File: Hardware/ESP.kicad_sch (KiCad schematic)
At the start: 22 parts, among them J2 USB_C_Receptacle_USB2.0_16P, U1 ESP32-C6-MINI-1/U, U2 TPS2115ADRBR, U8 LT1963AEST-3.3#TRPBF

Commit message: BPS-Leader Schematic completed (mostly)
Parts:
- J2: footprint UTSVT_Connectors:USB_C_Receptacle_GCT_USB4105-xx-A_16P_TopMnt_Horizontal -> UTSVT_Special:LeaderSOM
- U1: footprint (none) -> UTSVT_Special:ESP32-C6-MINI-1
- renumbered D3 to D11
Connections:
- no-connect marks 3 -> 8
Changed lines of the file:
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@@
 	)
 	(no_connect
+		(at 254 74.93)
+	)
+	(no_connect
 		(at 52.07 63.5)
 	)
@@
 	)
 	(no_connect
+		(at 254 69.85)
+	)
+	(no_connect
+		(at 254 64.77)
+	)
+	(no_connect
+		(at 254 67.31)
+	)
+	(no_connect
 		(at 52.07 60.96)
 	)
+	(no_connect
+		(at 254 72.39)
+	)
 	(wire
 		(pts
@@
 			)
 		)
-		(property "Footprint" "UTSVT_Connectors:USB_C_Receptacle_GCT_USB4105-xx-A_16P_TopMnt_Horizontal"
+		(property "Footprint" "UTSVT_Special:LeaderSOM"
 			(at 40.64 48.26 0)
 			(effects
@@
 			)
 		)
-		(property "Footprint" ""
+		(property "Footprint" "UTSVT_Special:ESP32-C6-MINI-1"
 			(at 228.6 24.13 0)
 			(effects
@@
 		(dnp no)
 		(fields_autoplaced yes)
-		(property "Reference" "D3"
+		(property "Reference" "D11"
 			(at 45.72 170.4974 90)
 			(effects
@@
 			(project "BPS-Leader"
 				(path "/fb37da34-e420-4994-8cc1-079e8c0fa48e/dabc680e-023d-4bcf-9356-bacd091b1cc9"
-					(reference "D3")
+					(reference "D11")
 					(unit 1)
 				)

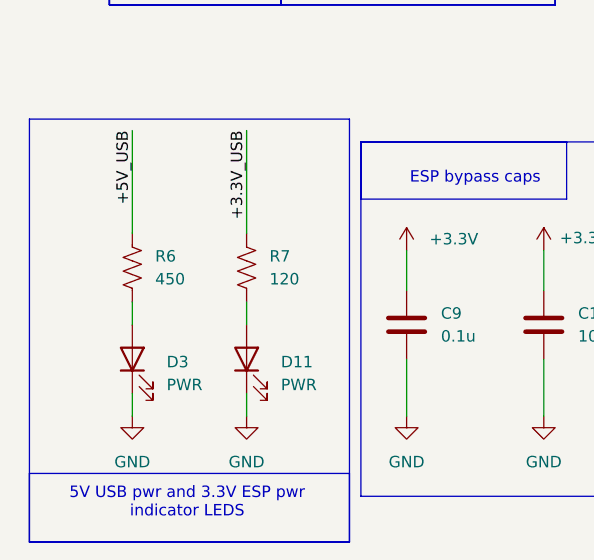
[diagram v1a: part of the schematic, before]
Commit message: added fuse, made kiCad Sharepoint a submodule, added a pulldown, added test-points
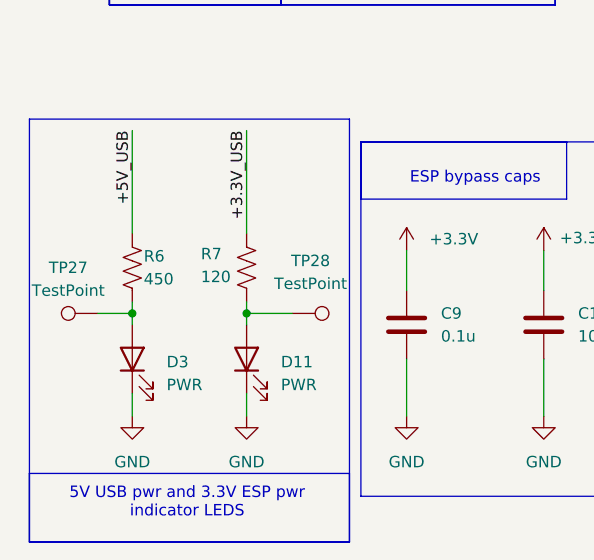
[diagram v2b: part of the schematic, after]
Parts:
- added TP27, TP28: TestPoint, symbol Connector:TestPoint
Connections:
- net at D3.2 (A), R6.2: now also TP27.1
- net at D11.2 (A), R7.2: now also TP28.1
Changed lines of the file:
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@@
 	)
 	(junction
+		(at 41.91 165.1)
+		(diameter 0)
+		(color 0 0 0 0)
+	)
+	(junction
 		(at 36.83 73.66)
 		(diameter 0)
@@
 		(color 0 0 0 0)
 	)
+	(junction
+		(at 29.21 165.1)
+		(diameter 0)
+		(color 0 0 0 0)
+	)
 	(no_connect
 		(at 254 74.93)
@@
 	(wire
 		(pts
+			(xy 41.91 165.1) (xy 41.91 166.37)
+		)
+		(stroke
+			(width 0)
+			(type default)
+		)
+	)
+	(wire
+		(pts
 			(xy 107.315 115.57) (xy 107.315 118.745)
 		)
@@
 	(wire
 		(pts
-			(xy 41.91 163.83) (xy 41.91 166.37)
+			(xy 41.91 163.83) (xy 41.91 165.1)
+		)
+		(stroke
+			(width 0)
+			(type default)
+		)
+	)
+	(wire
+		(pts
+			(xy 41.91 165.1) (xy 46.99 165.1)
 		)
 		(stroke
@@
 	(wire
 		(pts
-			(xy 29.21 163.83) (xy 29.21 166.37)
+			(xy 29.21 163.83) (xy 29.21 165.1)
 		)
 		(stroke
@@
 	(wire
 		(pts
+			(xy 25.4 165.1) (xy 29.21 165.1)
+		)
+		(stroke
+			(width 0)
+			(type default)
+		)
+	)
+	(wire
+		(pts
 			(xy 54.61 53.34) (xy 63.5 53.34)
 		)
@@
 	(wire
 		(pts
+			(xy 29.21 165.1) (xy 29.21 166.37)
+		)
+		(stroke
+			(width 0)
+			(type default)
+		)
+	)
+	(wire
+		(pts
 			(xy 41.91 144.78) (xy 41.91 156.21)
 		)
@@
 		(on_board yes)
 		(dnp no)
-		(fields_autoplaced yes)
 		(property "Reference" "R6"
-			(at 31.75 158.7499 0)
+			(at 30.48 158.75 0)
 			(effects
 				(font
@@
 		)
 		(property "Value" "450"
-			(at 31.75 161.2899 0)
+			(at 30.48 161.29 0)
 			(effects
 				(font
@@
 		(on_board yes)
 		(dnp no)
-		(fields_autoplaced yes)
 		(property "Reference" "R7"
-			(at 44.45 158.7499 0)
+			(at 36.83 158.496 0)
 			(effects
 				(font
@@
 		)
 		(property "Value" "120"
-			(at 44.45 161.2899 0)
+			(at 36.83 161.036 0)
 			(effects
 				(font
@@
 	)
 	(symbol
+		(lib_id "Connector:TestPoint")
+		(at 25.4 165.1 90)
+		(unit 1)
+		(exclude_from_sim no)
+		(in_bom yes)
+		(on_board yes)
+		(dnp no)
+		(fields_autoplaced yes)
+		(property "Reference" "TP27"
+			(at 22.098 160.02 90)
+			(effects
+				(font
+					(size 1.27 1.27)
+				)
+			)
+		)
+		(property "Value" "TestPoint"
+			(at 22.098 162.56 90)
+			(effects
+				(font
+					(size 1.27 1.27)
+				)
+			)
+		)
+		(property "Footprint" ""
+			(at 25.4 160.02 0)
+			(effects
+				(font
+					(size 1.27 1.27)
+				)
+				(hide yes)
+			)
+		)
+		(property "Datasheet" "~"
+			(at 25.4 160.02 0)
+			(effects
+				(font
+					(size 1.27 1.27)
+				)
+				(hide yes)
+			)
+		)
+		(property "Description" "test point"
+			(at 25.4 165.1 0)
+			(effects
+				(font
+					(size 1.27 1.27)
+				)
+				(hide yes)
+			)
+		)
+		(pin "1"
+		)
+		(instances
+			(project ""
+				(path "/fb37da34-e420-4994-8cc1-079e8c0fa48e/dabc680e-023d-4bcf-9356-bacd091b1cc9"
+					(reference "TP27")
+					(unit 1)
+				)
+			)
+		)
+	)
+	(symbol
 		(lib_id "Device:C")
 		(at 116.84 124.46 0)
@@
 					(unit 1)
 				)
+			)
+		)
+	)
+	(symbol
+		(lib_id "Connector:TestPoint")
+		(at 46.99 165.1 270)
+		(mirror x)
+		(unit 1)
+		(exclude_from_sim no)
+		(in_bom yes)
+		(on_board yes)
+		(dnp no)
+		(property "Reference" "TP28"
+			(at 49.022 159.258 90)
+			(effects
+				(font
+					(size 1.27 1.27)
+				)
+			)
+		)
+		(property "Value" "TestPoint"
+			(at 49.022 161.798 90)
+			(effects
+				(font
+					(size 1.27 1.27)
+				)
+			)
+		)
+		(property "Footprint" ""
+			(at 46.99 160.02 0)
+			(effects
+				(font
+					(size 1.27 1.27)
+				)
+				(hide yes)
+			)
+		)
+		(property "Datasheet" "~"
+			(at 46.99 160.02 0)
+			(effects
+				(font
+					(size 1.27 1.27)
+				)
+				(hide yes)
+			)
+		)
+		(property "Description" "test point"
+			(at 46.99 165.1 0)
+			(effects
+				(font
+					(size 1.27 1.27)
+				)
+				(hide yes)
+			)
+		)
+		(pin "1"
+		)
+		(instances
+			(project "BPS-Leader"
+				(path "/fb37da34-e420-4994-8cc1-079e8c0fa48e/dabc680e-023d-4bcf-9356-bacd091b1cc9"
+					(reference "TP28")
+					(unit 1)
+				)

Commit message: Small tweaks
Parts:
- added TP47, TP48: TestPoint, UTSVT_Special:TestPoint_HEX_3mmID, symbol Connector:TestPoint
- TP27, TP28: footprint (none) -> UTSVT_Special:TestPoint_HEX_3mmID
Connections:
- net +3.3V_USB: now also TP47.1
- net +5V_USB: now also TP48.1
- net +3.3V renamed +3.3V_ESP
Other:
- note added: "This is taken from VCU's ESP.kicad_sch (circa 09/09/2025) Only minimal cosmetic changes were made (i.e. 3V3 to +3.3V)"
- note removed: "This is taken from VCU's ESP.kicad_sch (circa 09/09/2025) Only minimal cosmetic changes were made (i.e. 3V3 to +3.3V) NOTE TO AUTHOR: CONFIRM PART DESIGNATION PARITY (i.e. J1 and U2)"
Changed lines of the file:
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@@
 	)
 	(rectangle
-		(start 17.78 143.51)
+		(start 16.002 143.51)
 		(end 53.34 190.5)
 		(stroke
@@
 		)
 	)
-	(text "This is taken from VCU's ESP.kicad_sch (circa 09/09/2025) \nOnly minimal cosmetic changes were made (i.e. 3V3 to +3.3V)\nNOTE TO AUTHOR: CONFIRM PART DESIGNATION PARITY (i.e. J1 and U2)"
+	(text "This is taken from VCU's ESP.kicad_sch (circa 09/09/2025) \nOnly minimal cosmetic changes were made (i.e. 3V3 to +3.3V)\n"
 		(exclude_from_sim no)
 		(at 214.884 172.212 0)
@@
 	)
 	(junction
+		(at 29.21 154.94)
+		(diameter 0)
+		(color 0 0 0 0)
+	)
+	(junction
 		(at 123.825 146.05)
 		(diameter 0)
@@
 	)
 	(junction
+		(at 41.91 153.67)
+		(diameter 0)
+		(color 0 0 0 0)
+	)
+	(junction
 		(at 116.84 118.11)
 		(diameter 0)
@@
 	(wire
 		(pts
+			(xy 41.91 153.67) (xy 41.91 156.21)
+		)
+		(stroke
+			(width 0)
+			(type default)
+		)
+	)
+	(wire
+		(pts
 			(xy 254 54.61) (xy 264.16 54.61)
 		)
@@
 	(wire
 		(pts
-			(xy 41.91 144.78) (xy 41.91 156.21)
+			(xy 41.91 144.78) (xy 41.91 153.67)
 		)
 		(stroke
@@
 	(wire
 		(pts
+			(xy 26.67 154.94) (xy 29.21 154.94)
+		)
+		(stroke
+			(width 0)
+			(type default)
+		)
+	)
+	(wire
+		(pts
 			(xy 226.06 85.09) (xy 226.06 90.17)
 		)
@@
 	(wire
 		(pts
-			(xy 29.21 144.78) (xy 29.21 156.21)
+			(xy 29.21 144.78) (xy 29.21 154.94)
 		)
 		(stroke
@@
 	(wire
 		(pts
+			(xy 29.21 154.94) (xy 29.21 156.21)
+		)
+		(stroke
+			(width 0)
+			(type default)
+		)
+	)
+	(wire
+		(pts
 			(xy 250.19 118.745) (xy 260.35 118.745)
 		)
@@
 		)
 	)
+	(wire
+		(pts
+			(xy 44.45 153.67) (xy 41.91 153.67)
+		)
+		(stroke
+			(width 0)
+			(type default)
+		)
+	)
 	(label "IO12"
 		(at 187.96 41.91 0)
@@
 			)
 		)
-		(property "Value" "+3.3V"
+		(property "Value" "+3.3V_ESP"
 			(at 226.06 17.78 0)
 			(effects
@@
 	)
 	(symbol
+		(lib_id "Connector:TestPoint")
+		(at 26.67 154.94 90)
+		(unit 1)
+		(exclude_from_sim no)
+		(in_bom yes)
+		(on_board yes)
+		(dnp no)
+		(property "Reference" "TP48"
+			(at 20.574 150.622 90)
+			(effects
+				(font
+					(size 1.27 1.27)
+				)
+			)
+		)
+		(property "Value" "TestPoint"
+			(at 21.082 152.908 90)
+			(effects
+				(font
+					(size 1.27 1.27)
+				)
+			)
+		)
+		(property "Footprint" "UTSVT_Special:TestPoint_HEX_3mmID"
+			(at 26.67 149.86 0)
+			(effects
+				(font
+					(size 1.27 1.27)
+				)
+				(hide yes)
+			)
+		)
+		(property "Datasheet" "~"
+			(at 26.67 149.86 0)
+			(effects
+				(font
+					(size 1.27 1.27)
+				)
+				(hide yes)
+			)
+		)
+		(property "Description" "test point"
+			(at 26.67 154.94 0)
+			(effects
+				(font
+					(size 1.27 1.27)
+				)
+				(hide yes)
+			)
+		)
+		(pin "1"
+		)
+		(instances
+			(project "BPS-Leader"
+				(path "/fb37da34-e420-4994-8cc1-079e8c0fa48e/dabc680e-023d-4bcf-9356-bacd091b1cc9"
+					(reference "TP48")
+					(unit 1)
+				)
+			)
+		)
+	)
+	(symbol
 		(lib_id "Device:R_US")
 		(at 29.21 160.02 0)
@@
 			)
 		)
-		(property "Value" "+3.3V"
-			(at 182.245 114.2999 0)
+		(property "Value" "+3.3V_ESP"
+			(at 176.784 111.76 0)
 			(effects
 				(font
@@
 			)
 		)
-		(property "Footprint" ""
+		(property "Footprint" "UTSVT_Special:TestPoint_HEX_3mmID"
 			(at 25.4 160.02 0)
 			(effects
@@
 		(dnp no)
 		(fields_autoplaced yes)
-		(property "Reference" "#PWR070"
+		(property "Reference" "#+3.3V_ESP0101"
 			(at 59.69 161.925 0)
 			(effects
@@
 			)
 		)
-		(property "Value" "+3.3V"
+		(property "Value" "+3.3V_ESP"
 			(at 62.23 156.8449 0)
 			(effects
@@
 			(project "BPS-Leader"
 				(path "/fb37da34-e420-4994-8cc1-079e8c0fa48e/dabc680e-023d-4bcf-9356-bacd091b1cc9"
-					(reference "#PWR070")
+					(reference "#+3.3V_ESP0101")
 					(unit 1)
 				)
@@
 	)
 	(symbol
+		(lib_id "Connector:TestPoint")
+		(at 44.45 153.67 270)
+		(mirror x)
+		(unit 1)
+		(exclude_from_sim no)
+		(in_bom yes)
+		(on_board yes)
+		(dnp no)
+		(property "Reference" "TP47"
+			(at 46.482 147.828 90)
+			(effects
+				(font
+					(size 1.27 1.27)
+				)
+			)
+		)
+		(property "Value" "TestPoint"
+			(at 46.482 150.368 90)
+			(effects
+				(font
+					(size 1.27 1.27)
+				)
+			)
+		)
+		(property "Footprint" "UTSVT_Special:TestPoint_HEX_3mmID"
+			(at 44.45 148.59 0)
+			(effects
+				(font
+					(size 1.27 1.27)
+				)
+				(hide yes)
+			)
+		)
+		(property "Datasheet" "~"
+			(at 44.45 148.59 0)
+			(effects
+				(font
+					(size 1.27 1.27)
+				)
+				(hide yes)
+			)
+		)
+		(property "Description" "test point"
+			(at 44.45 153.67 0)
+			(effects
+				(font
+					(size 1.27 1.27)
+				)
+				(hide yes)
+			)
+		)
+		(pin "1"
+		)
+		(instances
+			(project "BPS-Leader"
+				(path "/fb37da34-e420-4994-8cc1-079e8c0fa48e/dabc680e-023d-4bcf-9356-bacd091b1cc9"
+					(reference "TP47")
+					(unit 1)
+				)
+			)
+		)
+	)
+	(symbol
 		(lib_id "power:GND")
 		(at 74.93 176.53 0)
@@
 			)
 		)
-		(property "Footprint" ""
+		(property "Footprint" "UTSVT_Special:TestPoint_HEX_3mmID"
 			(at 46.99 160.02 0)
 			(effects
@@
 			)
 		)
-		(property "Value" "+3.3V"
+		(property "Value" "+3.3V_ESP"
 			(at 76.708 156.718 0)
 			(effects

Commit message: Very, very intial layout designed. Many issues. Too bad!
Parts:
- removed TP27, TP28: TestPoint, UTSVT_Special:TestPoint_HEX_3mmID, symbol Connector:TestPoint
- J2: footprint UTSVT_Special:LeaderSOM -> UTSVT_Connectors:USB_C_Receptacle_GCT_USB4105-xx-A_16P_TopMnt_Horizontal
- TP47, TP48: footprint UTSVT_Special:TestPoint_HEX_3mmID -> TestPoint:TestPoint_Pad_1.0x1.0mm
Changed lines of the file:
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@@
 	)
 	(junction
-		(at 41.91 165.1)
-		(diameter 0)
-		(color 0 0 0 0)
-	)
-	(junction
 		(at 36.83 73.66)
 		(diameter 0)
@@
 		(color 0 0 0 0)
 	)
-	(junction
-		(at 29.21 165.1)
-		(diameter 0)
-		(color 0 0 0 0)
-	)
 	(no_connect
 		(at 254 74.93)
@@
 	(wire
 		(pts
-			(xy 41.91 165.1) (xy 41.91 166.37)
+			(xy 41.91 163.83) (xy 41.91 166.37)
 		)
 		(stroke
@@
 	(wire
 		(pts
-			(xy 41.91 163.83) (xy 41.91 165.1)
-		)
-		(stroke
-			(width 0)
-			(type default)
-		)
-	)
-	(wire
-		(pts
-			(xy 41.91 165.1) (xy 46.99 165.1)
-		)
-		(stroke
-			(width 0)
-			(type default)
-		)
-	)
-	(wire
-		(pts
 			(xy 123.825 125.73) (xy 123.825 146.05)
 		)
@@
 	(wire
 		(pts
-			(xy 29.21 163.83) (xy 29.21 165.1)
+			(xy 29.21 163.83) (xy 29.21 166.37)
 		)
 		(stroke
@@
 	(wire
 		(pts
-			(xy 25.4 165.1) (xy 29.21 165.1)
-		)
-		(stroke
-			(width 0)
-			(type default)
-		)
-	)
-	(wire
-		(pts
 			(xy 54.61 53.34) (xy 63.5 53.34)
 		)
@@
 	(wire
 		(pts
-			(xy 29.21 165.1) (xy 29.21 166.37)
-		)
-		(stroke
-			(width 0)
-			(type default)
-		)
-	)
-	(wire
-		(pts
 			(xy 41.91 144.78) (xy 41.91 153.67)
 		)
@@
 	(wire
 		(pts
-			(xy 74.93 158.115) (xy 74.93 162.56)
+			(xy 74.93 157.48) (xy 74.93 162.56)
 		)
 		(stroke
@@
 		(dnp no)
 		(fields_autoplaced yes)
-		(property "Reference" "#PWR06"
+		(property "Reference" "#PWR0150"
 			(at 226.06 26.67 0)
 			(effects
@@
 			(project ""
 				(path "/fb37da34-e420-4994-8cc1-079e8c0fa48e/dabc680e-023d-4bcf-9356-bacd091b1cc9"
-					(reference "#PWR06")
+					(reference "#PWR0150")
 					(unit 1)
 				)
@@
 			)
 		)
-		(property "Footprint" "UTSVT_Special:TestPoint_HEX_3mmID"
+		(property "Footprint" "TestPoint:TestPoint_Pad_1.0x1.0mm"
 			(at 26.67 149.86 0)
 			(effects
@@
 			)
 		)
-		(property "Footprint" "UTSVT_Special:LeaderSOM"
+		(property "Footprint" "UTSVT_Connectors:USB_C_Receptacle_GCT_USB4105-xx-A_16P_TopMnt_Horizontal"
 			(at 40.64 48.26 0)
 			(effects
@@
 	)
 	(symbol
-		(lib_id "Connector:TestPoint")
-		(at 25.4 165.1 90)
-		(unit 1)
-		(exclude_from_sim no)
-		(in_bom yes)
-		(on_board yes)
-		(dnp no)
-		(fields_autoplaced yes)
-		(property "Reference" "TP27"
-			(at 22.098 160.02 90)
-			(effects
-				(font
-					(size 1.27 1.27)
-				)
-			)
-		)
-		(property "Value" "TestPoint"
-			(at 22.098 162.56 90)
-			(effects
-				(font
-					(size 1.27 1.27)
-				)
-			)
-		)
-		(property "Footprint" "UTSVT_Special:TestPoint_HEX_3mmID"
-			(at 25.4 160.02 0)
-			(effects
-				(font
-					(size 1.27 1.27)
-				)
-				(hide yes)
-			)
-		)
-		(property "Datasheet" "~"
-			(at 25.4 160.02 0)
-			(effects
-				(font
-					(size 1.27 1.27)
-				)
-				(hide yes)
-			)
-		)
-		(property "Description" "test point"
-			(at 25.4 165.1 0)
-			(effects
-				(font
-					(size 1.27 1.27)
-				)
-				(hide yes)
-			)
-		)
-		(pin "1"
-		)
-		(instances
-			(project ""
-				(path "/fb37da34-e420-4994-8cc1-079e8c0fa48e/dabc680e-023d-4bcf-9356-bacd091b1cc9"
-					(reference "TP27")
-					(unit 1)
-				)
-			)
-		)
-	)
-	(symbol
 		(lib_id "Device:C")
 		(at 116.84 124.46 0)
@@
 		(on_board yes)
 		(dnp no)
-		(fields_autoplaced yes)
-		(property "Reference" "#+3.3V_ESP0101"
+		(property "Reference" "#PWR0133"
 			(at 59.69 161.925 0)
 			(effects
@@
 		)
 		(property "Value" "+3.3V_ESP"
-			(at 62.23 156.8449 0)
+			(at 63.246 154.432 0)
 			(effects
 				(font
 					(size 1.27 1.27)
 				)
-				(justify left)
 			)
 		)
@@
 			(project "BPS-Leader"
 				(path "/fb37da34-e420-4994-8cc1-079e8c0fa48e/dabc680e-023d-4bcf-9356-bacd091b1cc9"
-					(reference "#+3.3V_ESP0101")
+					(reference "#PWR0133")
 					(unit 1)
 				)
@@
 			)
 		)
-		(property "Footprint" "UTSVT_Special:TestPoint_HEX_3mmID"
+		(property "Footprint" "TestPoint:TestPoint_Pad_1.0x1.0mm"
 			(at 44.45 148.59 0)
 			(effects
@@
 	)
 	(symbol
-		(lib_id "Connector:TestPoint")
-		(at 46.99 165.1 270)
-		(mirror x)
-		(unit 1)
-		(exclude_from_sim no)
-		(in_bom yes)
-		(on_board yes)
-		(dnp no)
-		(property "Reference" "TP28"
-			(at 49.022 159.258 90)
-			(effects
-				(font
-					(size 1.27 1.27)
-				)
-			)
-		)
-		(property "Value" "TestPoint"
-			(at 49.022 161.798 90)
-			(effects
-				(font
-					(size 1.27 1.27)
-				)
-			)
-		)
-		(property "Footprint" "UTSVT_Special:TestPoint_HEX_3mmID"
-			(at 46.99 160.02 0)
-			(effects
-				(font
-					(size 1.27 1.27)
-				)
-				(hide yes)
-			)
-		)
-		(property "Datasheet" "~"
-			(at 46.99 160.02 0)
-			(effects
-				(font
-					(size 1.27 1.27)
-				)
-				(hide yes)
-			)
-		)
-		(property "Description" "test point"
-			(at 46.99 165.1 0)
-			(effects
-				(font
-					(size 1.27 1.27)
-				)
-				(hide yes)
-			)
-		)
-		(pin "1"
-		)
-		(instances
-			(project "BPS-Leader"
-				(path "/fb37da34-e420-4994-8cc1-079e8c0fa48e/dabc680e-023d-4bcf-9356-bacd091b1cc9"
-					(reference "TP28")
-					(unit 1)
-				)
-			)
-		)
-	)
-	(symbol
 		(lib_id "power:+3V3")
-		(at 74.93 158.115 0)
+		(at 74.93 157.48 0)
 		(unit 1)
 		(exclude_from_sim no)
@@
 		(on_board yes)
 		(dnp no)
-		(property "Reference" "#PWR071"
-			(at 74.93 161.925 0)
+		(property "Reference" "#PWR06"
+			(at 74.93 161.29 0)
 			(effects
 				(font
@@
 		)
 		(property "Value" "+3.3V_ESP"
-			(at 76.708 156.718 0)
+			(at 77.47 153.924 0)
 			(effects
 				(font
 					(size 1.27 1.27)
 				)
-				(justify left)
 			)
 		)
 		(property "Footprint" ""
-			(at 74.93 158.115 0)
+			(at 74.93 157.48 0)
 			(effects
 				(font
@@
 		)
 		(property "Datasheet" ""
-			(at 74.93 158.115 0)
+			(at 74.93 157.48 0)
 			(effects
 				(font
@@
 		)
 		(property "Description" "Power symbol creates a global label with name \"+3V3\""
-			(at 74.93 158.115 0)
+			(at 74.93 157.48 0)
 			(effects
 				(font
@@
 			(project "BPS-Leader"
 				(path "/fb37da34-e420-4994-8cc1-079e8c0fa48e/dabc680e-023d-4bcf-9356-bacd091b1cc9"
-					(reference "#PWR071")
+					(reference "#PWR06")
 					(unit 1)
 				)

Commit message: small fixes
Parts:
- C12, C6, C8: Manufactuerer (none) -> TAIYO YUDEN; P/N UMK107B7104KAHT -> MLASH168SB7104KTNA01
- C9: Manufactuerer (none) -> TAIYO YUDEN; P/N (none) -> MLASH168SB7104KTNA01
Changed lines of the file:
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@@
 			)
 		)
-		(property "Datasheet" "~"
+		(property "Datasheet" "https://ds.yuden.co.jp/TYCOMPAS/or/download?pn=MLAST063SCG681JFNA01&fileType=CA"
 			(at 59.69 166.37 0)
 			(effects
@@
 			)
 		)
-		(property "Manufactuerer" ""
+		(property "Manufactuerer" "TAIYO YUDEN "
+			(at 59.69 166.37 0)
+			(effects
+				(font
+					(size 1.27 1.27)
+				)
+				(hide yes)
+			)
+		)
+		(property "P/N" "MLASH168SB7104KTNA01 "
 			(at 59.69 166.37 0)
 			(effects
@@
 			)
 		)
-		(property "Datasheet" "~"
+		(property "Datasheet" "https://ds.yuden.co.jp/TYCOMPAS/or/download?pn=MLAST063SCG681JFNA01&fileType=CA"
 			(at 179.705 127 0)
 			(effects
@@
 			)
 		)
-		(property "P/N" "UMK107B7104KAHT "
+		(property "P/N" "MLASH168SB7104KTNA01 "
 			(at 179.705 127 0)
 			(effects
@@
 			)
 		)
-		(property "Manufactuerer" ""
+		(property "Manufactuerer" "TAIYO YUDEN "
 			(at 179.705 127 0)
 			(effects
@@
 			)
 		)
-		(property "Datasheet" "~"
+		(property "Datasheet" "https://ds.yuden.co.jp/TYCOMPAS/or/download?pn=MLAST063SCG681JFNA01&fileType=CA"
 			(at 116.84 124.46 0)
 			(effects
@@
 			)
 		)
-		(property "P/N" "UMK107B7104KAHT "
+		(property "P/N" "MLASH168SB7104KTNA01 "
 			(at 116.84 124.46 0)
 			(effects
@@
 			)
 		)
-		(property "Manufactuerer" ""
+		(property "Manufactuerer" "TAIYO YUDEN "
 			(at 116.84 124.46 0)
 			(effects
@@
 			)
 		)
-		(property "Datasheet" "~"
+		(property "Datasheet" "https://ds.yuden.co.jp/TYCOMPAS/or/download?pn=MLAST063SCG681JFNA01&fileType=CA"
 			(at 107.315 122.555 0)
 			(effects
@@
 			)
 		)
-		(property "P/N" "UMK107B7104KAHT "
+		(property "P/N" "MLASH168SB7104KTNA01 "
 			(at 107.315 122.555 0)
 			(effects
@@
 			)
 		)
-		(property "Manufactuerer" ""
+		(property "Manufactuerer" "TAIYO YUDEN "
 			(at 107.315 122.555 0)
 			(effects
